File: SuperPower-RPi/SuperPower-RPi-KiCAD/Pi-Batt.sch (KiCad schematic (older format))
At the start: 0 parts

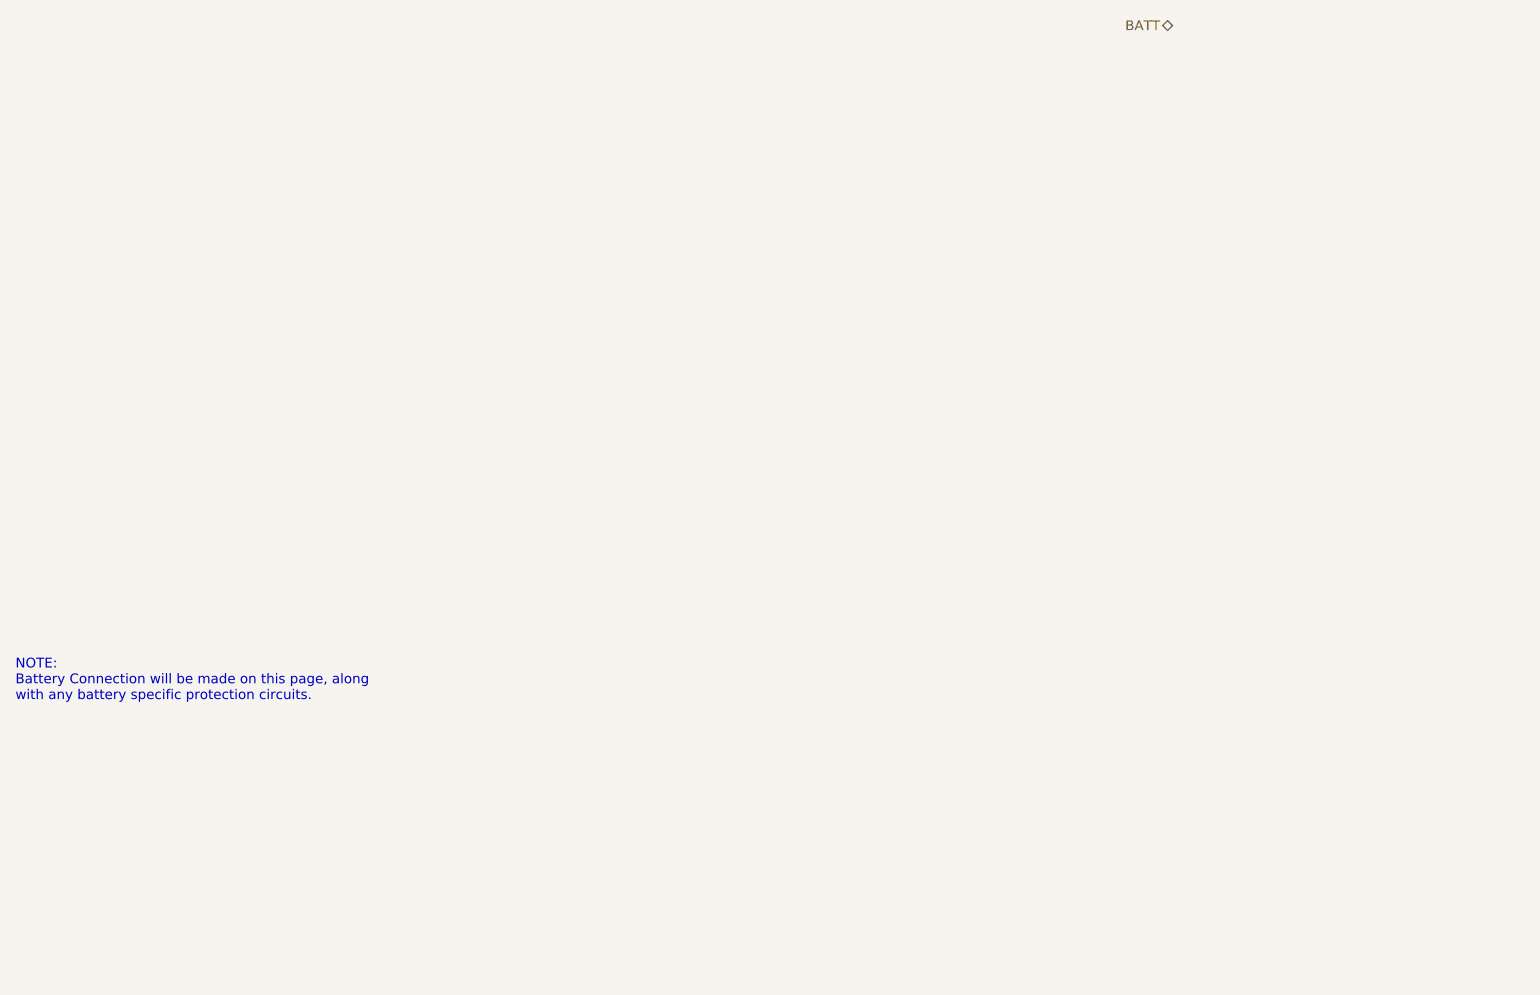
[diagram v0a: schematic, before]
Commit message: Added Battery reverse protection circuit for MWB.
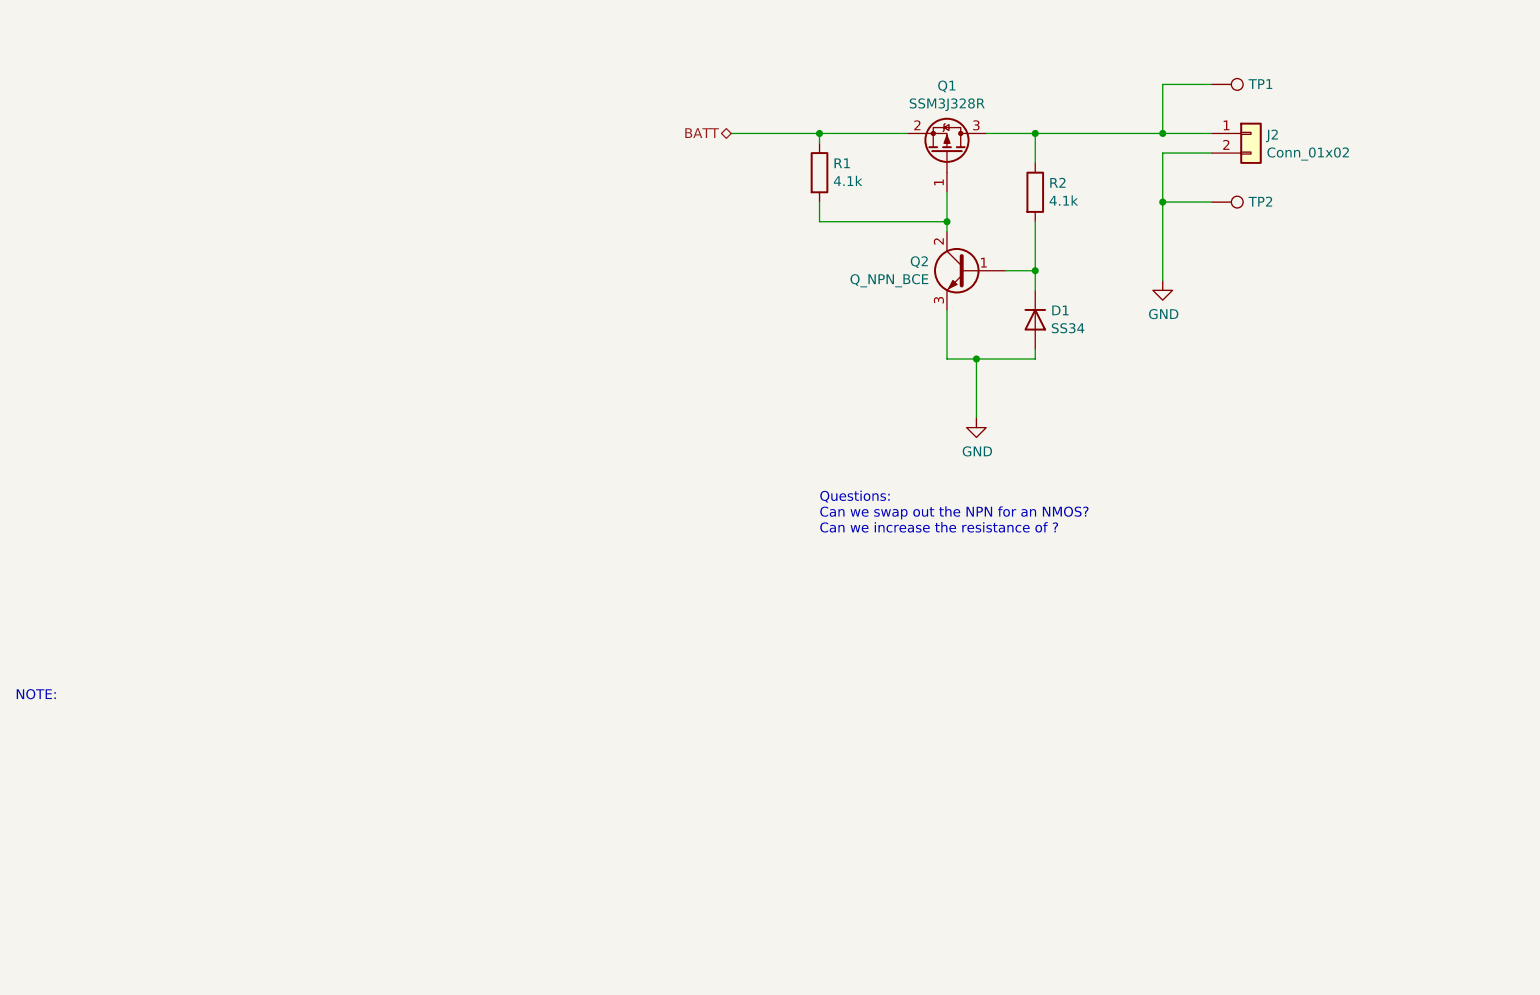
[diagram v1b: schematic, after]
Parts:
- added D1: SS34, symbol Device:D
- added J2: Conn_01x02, symbol Connector_Generic:Conn_01x02
- added Q1: SSM3J328R, symbol Device:Q_PMOS_GSD
- added Q2: Q_NPN_BCE, symbol Device:Q_NPN_BCE
- added R1, R2: 4.1k, symbol Device:R
- added TP1, TP2: TestPoint, symbol Connector:TestPoint
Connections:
- net BATT: now also Q1.2 (S), R1.1
- new net: J2.1 (Pin_1), Q1.3 (D), R2.1, TP1.1
- new net: D1.1 (K), Q2.1 (B), R2.2
- new net: Q1.1 (G), Q2.2 (C), R1.2
- new net GND: D1.2 (A), J2.2 (Pin_2), Q2.3 (E), TP2.1
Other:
- note added: "NOTE:\n"
- note added: "Questions:\nCan we swap out the NPN for an NMOS?\nCan we increase the resistance of ?"
- note removed: "NOTE:\nBattery Connection will be made on this page, along \nwith any battery specific protection circuits."
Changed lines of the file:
@@
 Comment4 ""
 $EndDescr
-Text HLabel 6950 2150 0    50   BiDi ~ 0
+Text HLabel 4700 2700 0    50   BiDi ~ 0
 BATT
 Text Notes 1050 5600 0    50   ~ 0
-NOTE:\nBattery Connection will be made on this page, along \nwith any battery specific protection circuits.
+NOTE:\n
+$Comp
+L Connector_Generic:Conn_01x02 J2
+U 1 1 5F701F7D
+P 7350 2700
+F 0 "J2" H 7430 2692 50  0000 L CNN
+F 1 "Conn_01x02" H 7430 2601 50  0000 L CNN
+F 2 "" H 7350 2700 50  0001 C CNN
+F 3 "~" H 7350 2700 50  0001 C CNN
+	1    7350 2700
+	1    0    0    -1
+$EndComp
+$Comp
+L Device:D D1
+U 1 1 5F702A8B
+P 6250 3650
+F 0 "D1" V 6204 3730 50  0000 L CNN
+F 1 "SS34" V 6295 3730 50  0000 L CNN
+F 2 "" H 6250 3650 50  0001 C CNN
+F 3 "~" H 6250 3650 50  0001 C CNN
+	1    6250 3650
+	0    1    1    0
+$EndComp
+$Comp
+L power:GND #PWR02
+U 1 1 5F703173
+P 5950 4150
+F 0 "#PWR02" H 5950 3900 50  0001 C CNN
+F 1 "GND" H 5955 3977 50  0000 C CNN
+F 2 "" H 5950 4150 50  0001 C CNN
+F 3 "" H 5950 4150 50  0001 C CNN
+	1    5950 4150
+	1    0    0    -1
+$EndComp
+$Comp
+L Device:R R2
+U 1 1 5F7036D1
+P 6250 3000
+F 0 "R2" H 6320 3046 50  0000 L CNN
+F 1 "4.1k" H 6320 2955 50  0000 L CNN
+F 2 "" V 6180 3000 50  0001 C CNN
+F 3 "~" H 6250 3000 50  0001 C CNN
+	1    6250 3000
+	1    0    0    -1
+$EndComp
+$Comp
+L Device:Q_PMOS_GSD Q1
+U 1 1 5F704F9B
+P 5800 2800
+F 0 "Q1" V 6142 2800 50  0000 C CNN
+F 1 "SSM3J328R" V 6051 2800 50  0000 C CNN
+F 2 "" H 6000 2900 50  0001 C CNN
+F 3 "~" H 5800 2800 50  0001 C CNN
+	1    5800 2800
+	0    1    -1   0
+$EndComp
+Wire Wire Line
+	6250 2700 6250 2850
+Wire Wire Line
+	6000 2700 6250 2700
+Connection ~ 6250 2700
+Wire Wire Line
+	6250 2700 6900 2700
+$Comp
+L Device:Q_NPN_BCE Q2
+U 1 1 5F708549
+P 5900 3400
+F 0 "Q2" H 6091 3446 50  0000 L CNN
+F 1 "Q_NPN_BCE" H 6091 3355 50  0000 L CNN
+F 2 "" H 6100 3500 50  0001 C CNN
+F 3 "~" H 5900 3400 50  0001 C CNN
+	1    5900 3400
+	-1   0    0    -1
+$EndComp
+Wire Wire Line
+	5800 3600 5800 3850
+Wire Wire Line
+	5800 3850 5950 3850
+Wire Wire Line
+	6250 3850 6250 3800
+Wire Wire Line
+	6250 3500 6250 3400
+Wire Wire Line
+	6100 3400 6250 3400
+Connection ~ 6250 3400
+Wire Wire Line
+	6250 3400 6250 3150
+Wire Wire Line
+	5800 3200 5800 3150
+Wire Wire Line
+	5950 4150 5950 3850
+Connection ~ 5950 3850
+Wire Wire Line
+	5950 3850 6250 3850
+$Comp
+L Device:R R1
+U 1 1 5F709FD7
+P 5150 2900
+F 0 "R1" H 5220 2946 50  0000 L CNN
+F 1 "4.1k" H 5220 2855 50  0000 L CNN
+F 2 "" V 5080 2900 50  0001 C CNN
+F 3 "~" H 5150 2900 50  0001 C CNN
+	1    5150 2900
+	1    0    0    -1
+$EndComp
+Wire Wire Line
+	5150 2750 5150 2700
+Wire Wire Line
+	5150 2700 5600 2700
+Wire Wire Line
+	5150 3050 5150 3150
+Wire Wire Line
+	5150 3150 5800 3150
+Connection ~ 5800 3150
+Wire Wire Line
+	5800 3150 5800 3000
+Wire Wire Line
+	4700 2700 5150 2700
+Connection ~ 5150 2700
+Text Notes 5150 4750 0    50   ~ 0
+Questions:\nCan we swap out the NPN for an NMOS?\nCan we increase the resistance of ?
+$Comp
+L power:GND #PWR03
+U 1 1 5F70F58A
+P 6900 3450
+F 0 "#PWR03" H 6900 3200 50  0001 C CNN
+F 1 "GND" H 6905 3277 50  0000 C CNN
+F 2 "" H 6900 3450 50  0001 C CNN
+F 3 "" H 6900 3450 50  0001 C CNN
+	1    6900 3450
+	1    0    0    -1
+$EndComp
+$Comp
+L Connector:TestPoint TP2
+U 1 1 5F70FBD7
+P 7150 3050
+F 0 "TP2" V 7150 3238 50  0000 L CNN
+F 1 "TestPoint" V 7195 3238 50  0001 L CNN
+F 2 "" H 7350 3050 50  0001 C CNN
+F 3 "~" H 7350 3050 50  0001 C CNN
+	1    7150 3050
+	0    1    1    0
+$EndComp
+$Comp
+L Connector:TestPoint TP1
+U 1 1 5F710403
+P 7150 2450
+F 0 "TP1" V 7150 2638 50  0000 L CNN
+F 1 "TestPoint" V 7195 2638 50  0001 L CNN
+F 2 "" H 7350 2450 50  0001 C CNN
+F 3 "~" H 7350 2450 50  0001 C CNN
+	1    7150 2450
+	0    1    1    0
+$EndComp
+Wire Wire Line
+	7150 2450 6900 2450
+Wire Wire Line
+	6900 2450 6900 2700
+Connection ~ 6900 2700
+Wire Wire Line
+	6900 2700 7150 2700
+Wire Wire Line
+	7150 3050 6900 3050
+Wire Wire Line
+	6900 3050 6900 3450
+Wire Wire Line
+	6900 3050 6900 2800
+Wire Wire Line
+	6900 2800 7150 2800
+Connection ~ 6900 3050
 $EndSCHEMATC

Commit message: Made a change to demo KiCAD.
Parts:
- R2: value 4.1k -> 10k
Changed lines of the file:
@@
 P 6250 3000
 F 0 "R2" H 6320 3046 50  0000 L CNN
-F 1 "4.1k" H 6320 2955 50  0000 L CNN
+F 1 "10k" H 6320 2955 50  0000 L CNN
 F 2 "" V 6180 3000 50  0001 C CNN
 F 3 "~" H 6250 3000 50  0001 C CNN

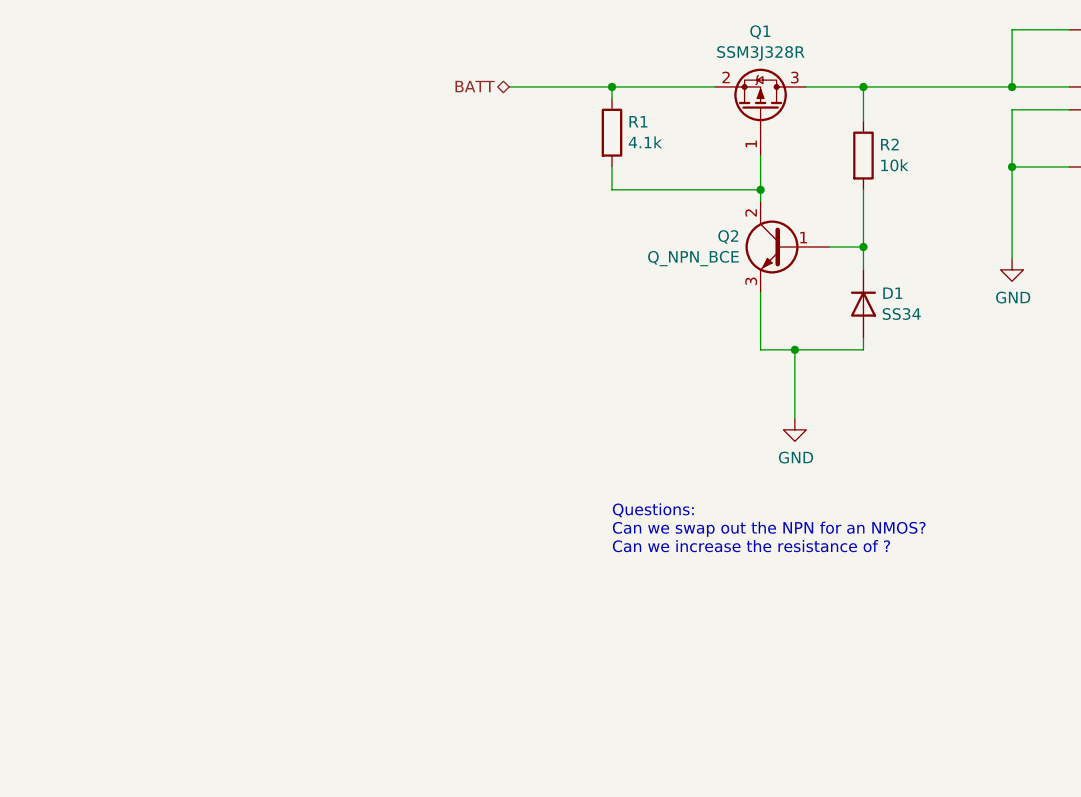
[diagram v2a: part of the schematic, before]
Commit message: Added charger circuitry, and updated boost converter.
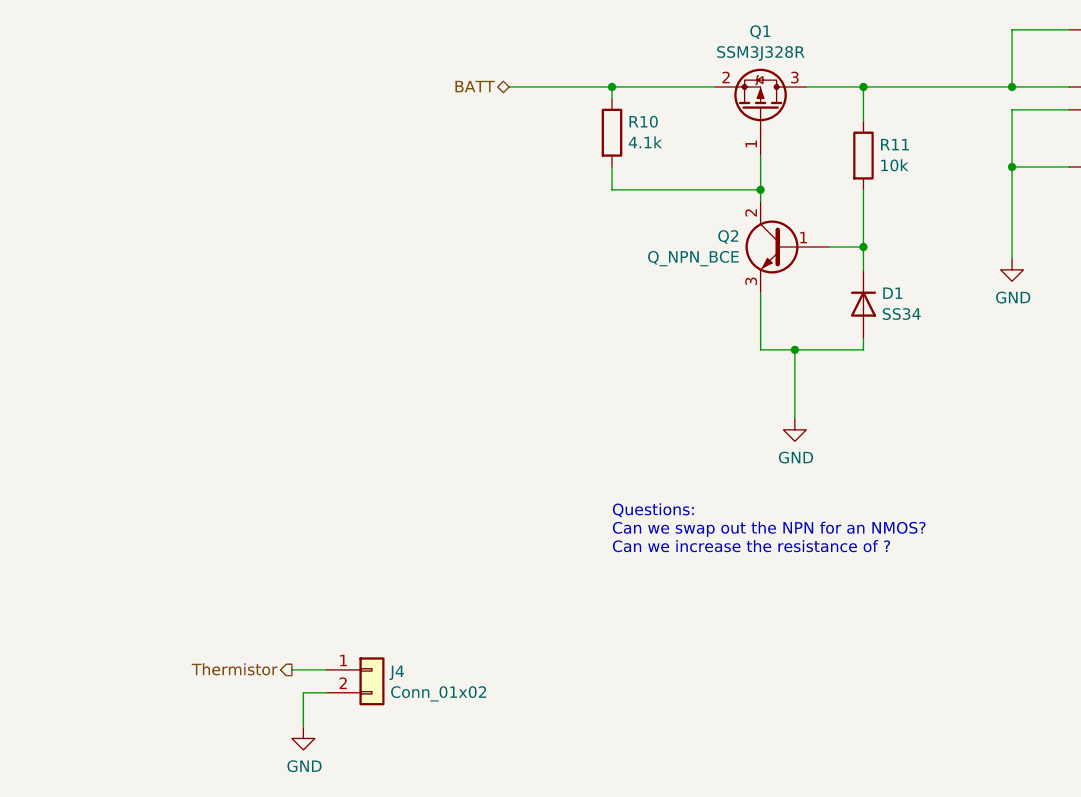
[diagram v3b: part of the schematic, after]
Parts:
- added J4: Conn_01x02, symbol Connector_Generic:Conn_01x02
- renumbered R1 to R10, R2 to R11
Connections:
- net GND: now also J4.2 (Pin_2)
- new net Thermistor: J4.1 (Pin_1)
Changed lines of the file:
@@
 $EndComp
 $Comp
-L power:GND #PWR02
+L power:GND #PWR0103
 U 1 1 5F703173
 P 5950 4150
-F 0 "#PWR02" H 5950 3900 50  0001 C CNN
+F 0 "#PWR0103" H 5950 3900 50  0001 C CNN
 F 1 "GND" H 5955 3977 50  0000 C CNN
 F 2 "" H 5950 4150 50  0001 C CNN
@@
 $EndComp
 $Comp
-L Device:R R2
+L Device:R R11
 U 1 1 5F7036D1
 P 6250 3000
-F 0 "R2" H 6320 3046 50  0000 L CNN
+F 0 "R11" H 6320 3046 50  0000 L CNN
 F 1 "10k" H 6320 2955 50  0000 L CNN
 F 2 "" V 6180 3000 50  0001 C CNN
@@
 	5950 3850 6250 3850
 $Comp
-L Device:R R1
+L Device:R R10
 U 1 1 5F709FD7
 P 5150 2900
-F 0 "R1" H 5220 2946 50  0000 L CNN
+F 0 "R10" H 5220 2946 50  0000 L CNN
 F 1 "4.1k" H 5220 2855 50  0000 L CNN
 F 2 "" V 5080 2900 50  0001 C CNN
@@
 Questions:\nCan we swap out the NPN for an NMOS?\nCan we increase the resistance of ?
 $Comp
-L power:GND #PWR03
+L power:GND #PWR0104
 U 1 1 5F70F58A
 P 6900 3450
-F 0 "#PWR03" H 6900 3200 50  0001 C CNN
+F 0 "#PWR0104" H 6900 3200 50  0001 C CNN
 F 1 "GND" H 6905 3277 50  0000 C CNN
 F 2 "" H 6900 3450 50  0001 C CNN
@@
 	6900 2800 7150 2800
 Connection ~ 6900 3050
+Text HLabel 3750 5250 0    50   Output ~ 0
+Thermistor
+$Comp
+L Connector_Generic:Conn_01x02 J4
+U 1 1 5F7ACDE2
+P 4100 5250
+F 0 "J4" H 4180 5242 50  0000 L CNN
+F 1 "Conn_01x02" H 4180 5151 50  0000 L CNN
+F 2 "" H 4100 5250 50  0001 C CNN
+F 3 "~" H 4100 5250 50  0001 C CNN
+	1    4100 5250
+	1    0    0    -1
+$EndComp
+Wire Wire Line
+	3900 5250 3750 5250
+$Comp
+L power:GND #PWR015
+U 1 1 5F7AD85C
+P 3800 5500
+F 0 "#PWR015" H 3800 5250 50  0001 C CNN
+F 1 "GND" H 3805 5327 50  0000 C CNN
+F 2 "" H 3800 5500 50  0001 C CNN
+F 3 "" H 3800 5500 50  0001 C CNN
+	1    3800 5500
+	1    0    0    -1
+$EndComp
+Wire Wire Line
+	3800 5500 3800 5350
+Wire Wire Line
+	3800 5350 3900 5350
 $EndSCHEMATC

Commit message: Updated components. Mostly caps and resistors.
(cherry picked from commit e921c80666429be92cc496d87bcbd557350196b5)
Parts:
- R10, R11: footprint (none) -> Resistor_SMD:R_0603_1608Metric
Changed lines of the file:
@@
 F 0 "R11" H 6320 3046 50  0000 L CNN
 F 1 "10k" H 6320 2955 50  0000 L CNN
-F 2 "" V 6180 3000 50  0001 C CNN
+F 2 "Resistor_SMD:R_0603_1608Metric" V 6180 3000 50  0001 C CNN
 F 3 "~" H 6250 3000 50  0001 C CNN
 	1    6250 3000
@@
 F 0 "R10" H 5220 2946 50  0000 L CNN
 F 1 "4.1k" H 5220 2855 50  0000 L CNN
-F 2 "" V 5080 2900 50  0001 C CNN
+F 2 "Resistor_SMD:R_0603_1608Metric" V 5080 2900 50  0001 C CNN
 F 3 "~" H 5150 2900 50  0001 C CNN
 	1    5150 2900
